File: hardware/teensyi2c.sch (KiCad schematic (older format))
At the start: 11 parts, among them J1 TEENSY3.2-72MHz, J2 OLED-I2C, J3 ADAFRUIT_BME280, U1 ESP-01v090

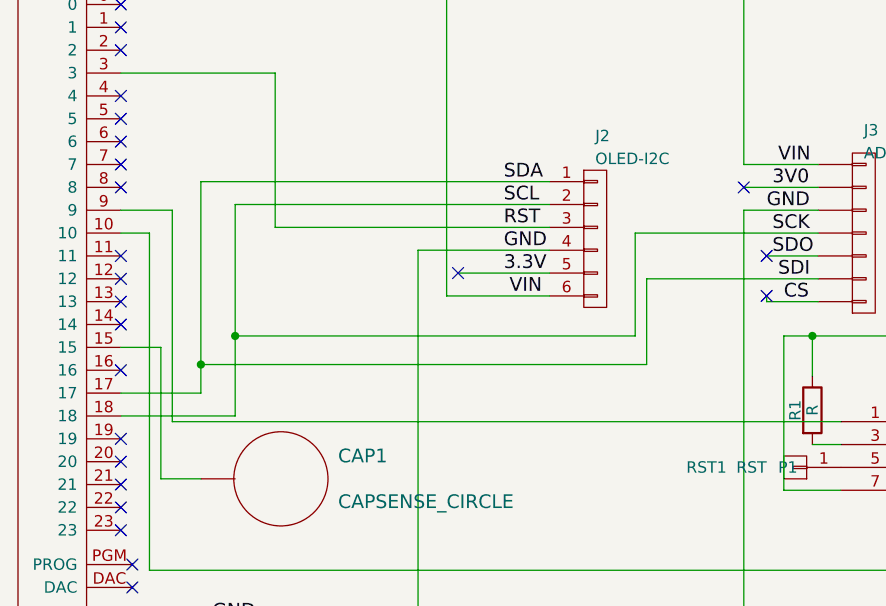
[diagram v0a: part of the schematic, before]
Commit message: fix i2c bus pins
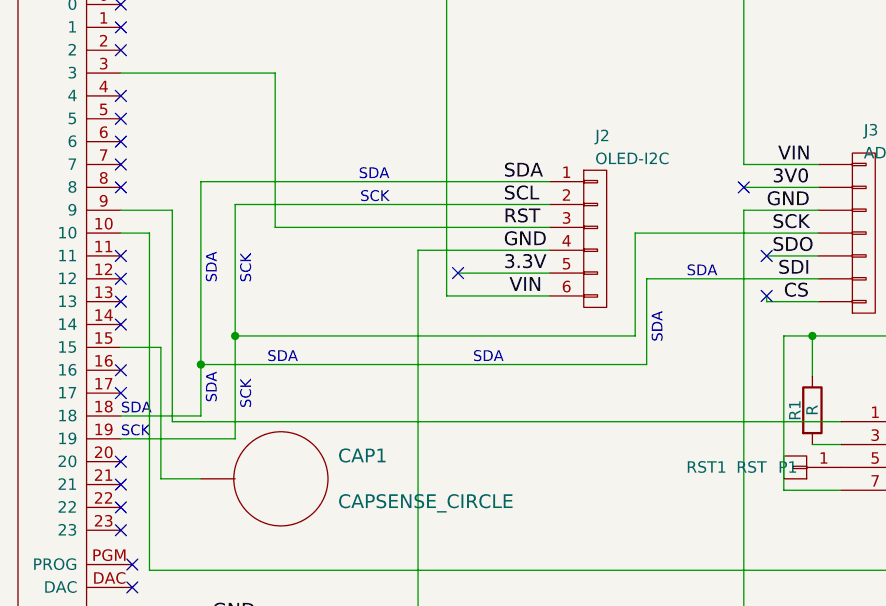
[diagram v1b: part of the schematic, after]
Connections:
- net SCK: now also J1.19; no longer J1.18
- net SDA: now also J1.18; no longer J1.17
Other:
- note added: "SCK"
- note added: "SDA"
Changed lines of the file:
@@
 	1    0    0    -1
 $EndComp
-Wire Wire Line
-	5825 3225 7350 3225
-Wire Wire Line
-	5975 3325 7350 3325
-Wire Wire Line
-	6150 3425 7350 3425
-Wire Wire Line
-	6775 3525 7350 3525
-Wire Wire Line
-	7350 3625 6950 3625
-Wire Wire Line
-	7350 3725 6900 3725
-Wire Wire Line
-	5825 3225 5825 4150
-Wire Wire Line
-	5825 4150 5475 4150
-Wire Wire Line
-	5975 3325 5975 4250
-Wire Wire Line
-	5975 4250 5475 4250
-Wire Wire Line
-	6150 3425 6150 2750
-Wire Wire Line
-	6150 2750 5475 2750
-Wire Wire Line
-	6775 3525 6775 5250
-Wire Wire Line
-	5475 5150 11050 5150
-Wire Wire Line
-	6900 3725 6900 2150
-Wire Wire Line
-	8525 3150 8200 3150
-Wire Wire Line
-	8200 3150 8200 2150
-Connection ~ 6900 2150
-Wire Wire Line
-	8525 3350 8200 3350
-Wire Wire Line
-	8200 3350 8200 5150
-Connection ~ 6775 5150
-Wire Wire Line
-	8525 3450 7725 3450
-Wire Wire Line
-	7725 3450 7725 3900
-Wire Wire Line
-	7725 3900 5975 3900
-Connection ~ 5975 3900
-Wire Wire Line
-	8525 3650 7775 3650
-Wire Wire Line
-	7775 3650 7775 4025
-Wire Wire Line
-	7775 4025 5825 4025
-Connection ~ 5825 4025
-Wire Wire Line
-	8525 3250 8200 3250
-Wire Wire Line
-	8300 3550 8525 3550
-Wire Wire Line
-	8525 3750 8300 3750
-Wire Wire Line
-	8300 3750 8300 3725
-Wire Wire Line
-	10525 4275 11050 4275
-Wire Wire Line
-	11050 4275 11050 5150
-Connection ~ 8200 5150
-Wire Wire Line
-	8625 4575 8375 4575
-Wire Wire Line
-	8375 4575 8375 3900
-Wire Wire Line
-	8375 3900 9725 3900
-Wire Wire Line
-	9725 3900 9725 2150
-Connection ~ 8200 2150
 $Comp
 L R R1
@@
 	1    0    0    -1
 $EndComp
-Wire Wire Line
-	8625 4375 8500 4375
-Wire Wire Line
-	8500 4075 8500 3900
-Connection ~ 8500 3900
-Wire Wire Line
-	5475 3350 5700 3350
-Wire Wire Line
-	5700 3350 5700 4275
-Wire Wire Line
-	5700 4275 8625 4275
-Wire Wire Line
-	5475 3450 5600 3450
-Wire Wire Line
-	5600 3450 5600 4925
-Wire Wire Line
-	5600 4925 10525 4925
-Wire Wire Line
-	10525 4925 10525 4575
 $Comp
 L HEADER-MALE-1POS-TH-1x01 RST1
@@
 	1    0    0    -1
 $EndComp
-Wire Wire Line
-	6775 5250 5475 5250
 $Comp
 L HEADER-MALE-1POS-TH-1x01 GND1
@@
 	0    -1   -1   0
 $EndComp
-Wire Wire Line
-	5700 2200 5525 2200
-Wire Wire Line
-	5700 2100 5700 2200
-Wire Wire Line
-	9725 2150 5700 2150
-Wire Wire Line
-	5525 2100 5700 2100
-Connection ~ 5700 2150
 NoConn ~ 8200 3250
-NoConn ~ 8300 3550
 NoConn ~ 8300 3725
 NoConn ~ 6950 3625
@@
 NoConn ~ 5475 3850
 NoConn ~ 5475 4050
-NoConn ~ 5475 4350
 NoConn ~ 5475 4450
 NoConn ~ 5475 4550
@@
 	1    0    0    -1
 $EndComp
+Text Notes 5475 4350 0    47   ~ 0
+SCK
+Text Notes 5475 4250 0    47   ~ 0
+SDA
+NoConn ~ 8300 3550
+Wire Wire Line
+	6150 3425 7350 3425
+Wire Wire Line
+	6775 3525 7350 3525
+Wire Wire Line
+	7350 3625 6950 3625
+Wire Wire Line
+	7350 3725 6900 3725
+Wire Wire Line
+	6150 3425 6150 2750
+Wire Wire Line
+	6150 2750 5475 2750
+Wire Wire Line
+	6775 3525 6775 5250
+Wire Wire Line
+	5475 5150 11050 5150
+Wire Wire Line
+	6900 3725 6900 2150
+Wire Wire Line
+	8525 3150 8200 3150
+Wire Wire Line
+	8200 3150 8200 2150
+Connection ~ 6900 2150
+Wire Wire Line
+	8525 3350 8200 3350
+Wire Wire Line
+	8200 3350 8200 5150
+Connection ~ 6775 5150
+Wire Wire Line
+	8525 3450 7725 3450
+Wire Wire Line
+	7725 3450 7725 3900
+Wire Wire Line
+	7725 3900 5975 3900
+Connection ~ 5975 3900
+Wire Wire Line
+	8525 3650 7775 3650
+Wire Wire Line
+	7775 3650 7775 4025
+Wire Wire Line
+	7775 4025 5825 4025
+Connection ~ 5825 4025
+Wire Wire Line
+	8525 3250 8200 3250
+Wire Wire Line
+	8300 3550 8525 3550
+Wire Wire Line
+	8525 3750 8300 3750
+Wire Wire Line
+	8300 3750 8300 3725
+Wire Wire Line
+	10525 4275 11050 4275
+Wire Wire Line
+	11050 4275 11050 5150
+Connection ~ 8200 5150
+Wire Wire Line
+	8625 4575 8375 4575
+Wire Wire Line
+	8375 4575 8375 3900
+Wire Wire Line
+	8375 3900 9725 3900
+Wire Wire Line
+	9725 3900 9725 2150
+Connection ~ 8200 2150
+Wire Wire Line
+	8625 4375 8500 4375
+Wire Wire Line
+	8500 4075 8500 3900
+Connection ~ 8500 3900
+Wire Wire Line
+	5475 3350 5700 3350
+Wire Wire Line
+	5700 3350 5700 4275
+Wire Wire Line
+	5700 4275 8625 4275
+Wire Wire Line
+	5475 3450 5600 3450
+Wire Wire Line
+	5600 3450 5600 4925
+Wire Wire Line
+	5600 4925 10525 4925
+Wire Wire Line
+	10525 4925 10525 4575
+Wire Wire Line
+	6775 5250 5475 5250
+Wire Wire Line
+	5700 2200 5525 2200
+Wire Wire Line
+	5700 2100 5700 2200
+Wire Wire Line
+	9725 2150 5700 2150
+Wire Wire Line
+	5525 2100 5700 2100
+Connection ~ 5700 2150
 Wire Wire Line
 	5475 3950 5650 3950
@@
 Wire Wire Line
 	5650 4525 5825 4525
+Wire Wire Line
+	5475 4250 5825 4250
+Wire Wire Line
+	5825 4250 5825 3225
+Wire Wire Line
+	5825 3225 7350 3225
+Text Notes 5900 4200 1    47   ~ 0
+SDA
+Text Notes 6250 4025 2    47   ~ 0
+SDA
+Text Notes 7150 4025 2    47   ~ 0
+SDA
+Text Notes 7850 3800 3    47   ~ 0
+SDA
+Text Notes 7950 3650 0    47   ~ 0
+SDA
+Wire Wire Line
+	5475 4350 5975 4350
+Wire Wire Line
+	5975 4350 5975 3325
+Wire Wire Line
+	5975 3325 7350 3325
+Text Notes 6050 4225 1    47   ~ 0
+SCK
+Text Notes 6050 3675 1    47   ~ 0
+SCK
+Text Notes 5900 3675 1    47   ~ 0
+SDA
+Text Notes 6650 3325 2    47   ~ 0
+SCK
+Text Notes 6650 3225 2    47   ~ 0
+SDA
+NoConn ~ 5475 4150
 $EndSCHEMATC
